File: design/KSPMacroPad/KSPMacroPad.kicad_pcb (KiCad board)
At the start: 2 copper layers, 95.2 x 112.5 mm, 72 parts, among them SW1 SW_Push, SW10 SW_Push, SW11 SW_Push, SW12 SW_Push, SW13 SW_Push, SW14 SW_Push, SW15 SW_Push, SW16 SW_Push, SW17 RotaryEncoder_Switch, SW18 RotaryEncoder_Switch, SW2 SW_Push, SW3 SW_Push, SW4 SW_Push, SW5 SW_Push, SW6 SW_Push, SW7 SW_Push, SW8 SW_Push, SW9 SW_Push, U1 MOUDLE-SEEEDUINO-XIAO

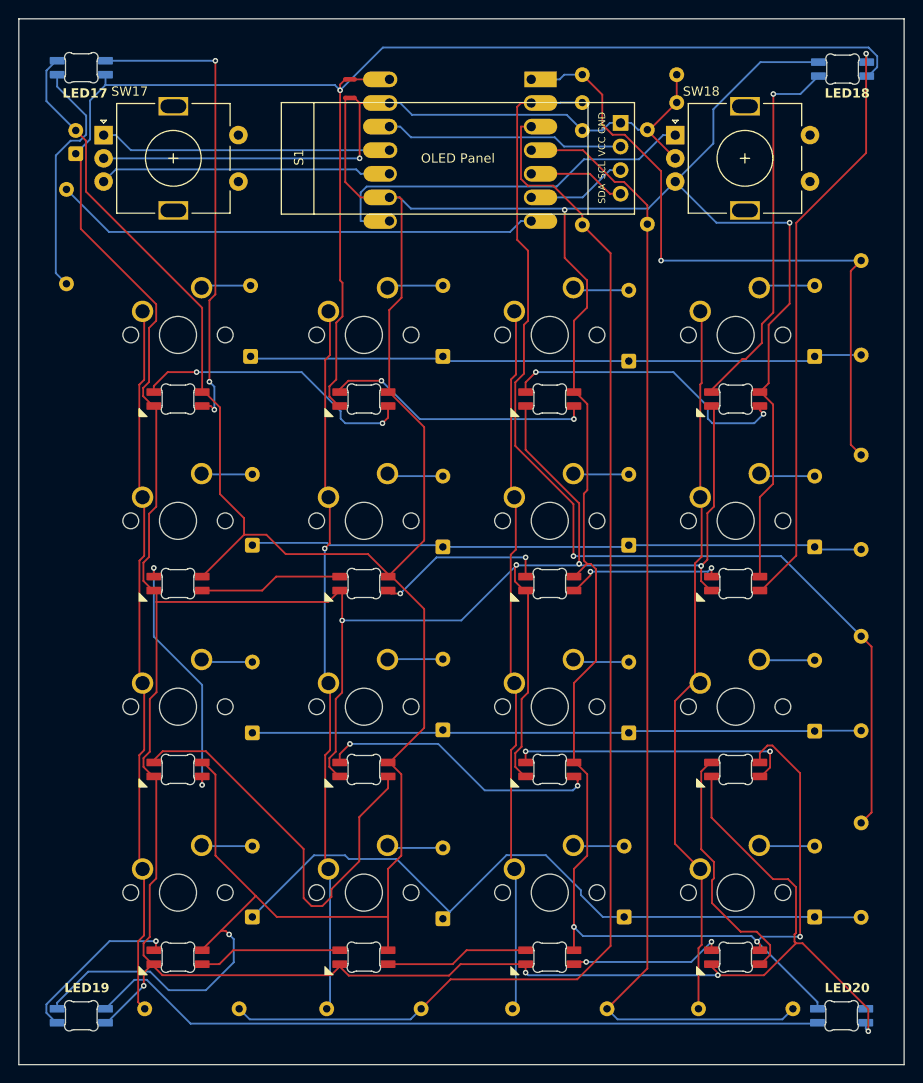
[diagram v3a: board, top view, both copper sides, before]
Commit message: silkscreen and sizine
fixed the sizing of the PCB and added some silkscreen text so the PCB is easier to configure once I build it irl
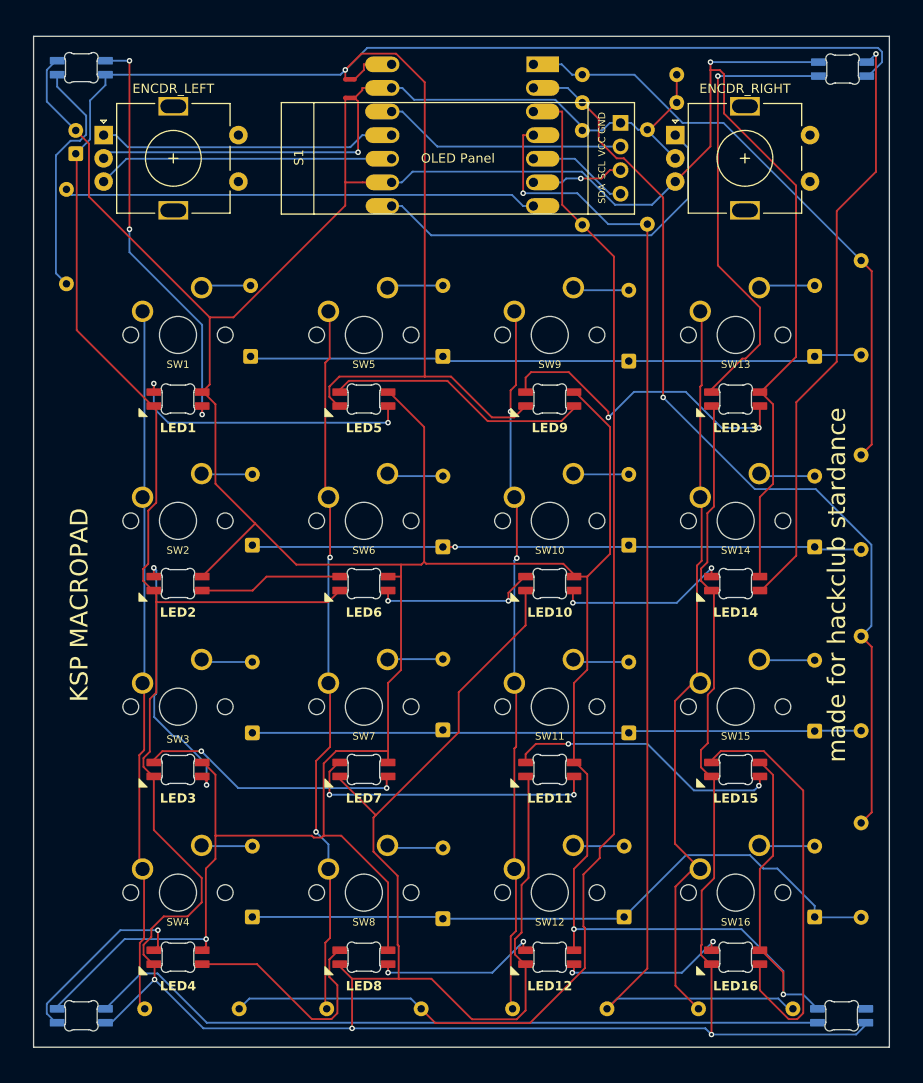
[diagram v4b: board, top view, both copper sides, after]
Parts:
- moved U1 1.63 mm to (115.6, 43.5)
- renumbered SW17 to ENCDR_LEFT, SW18 to ENCDR_RIGHT
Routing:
- net /LED_5V: track 498.6 -> 558.1 mm, vias 9 -> 4
- net Net-(LED15-DOUT): track 27.0 -> 45.3 mm
- net Net-(LED3-DOUT): track 45.7 -> 28.7 mm, vias 0 -> 2
- net /row3_4: track 114.7 -> 102.0 mm
- net Net-(LED4-DIN): track 15.4 -> 24.9 mm
- net Net-(LED13-DOUT): track 40.7 -> 49.1 mm
- net /row1_2: track 73.3 -> 65.9 mm, vias 1 -> 0
- net Net-(LED1-DIN): track 51.3 -> 44.8 mm
- net Net-(D12-K): track 77.4 -> 71.9 mm
- net /col3_4: track 124.1 -> 129.2 mm, vias 0 -> 1
- net Net-(LED13-DIN): track 31.6 -> 34.4 mm
- net Net-(LED12-DOUT): track 15.4 -> 17.9 mm, vias 0 -> 2
- net Net-(R4-Pad1): track 78.7 -> 80.7 mm
- net Net-(LED19-DIN): track 18.2 -> 20.1 mm
- net Net-(LED11-DIN): track 30.4 -> 32.3 mm
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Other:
- board size 95.2 x 112.5 mm -> 92.1 x 108.8 mm
- board text added: "KSP MACROPAD"
- board text added: "a mintythetechman project"
- board text added: "made for hackclub stardance"

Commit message: added M# mounting holes
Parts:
- added SCRW1: MountingHole_3.2mm_M3, MountingHole:MountingHole_3.2mm_M3, F.Cu at (73.5, 68.0)
- added SCRW2: MountingHole_3.2mm_M3, MountingHole:MountingHole_3.2mm_M3, F.Cu at (115.0, 95.5)
- added SCRW3: MountingHole_3.2mm_M3, MountingHole:MountingHole_3.2mm_M3, F.Cu at (158.0, 132.5)
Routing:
- net Net-(LED10-DOUT): track 17.5 -> 19.7 mm

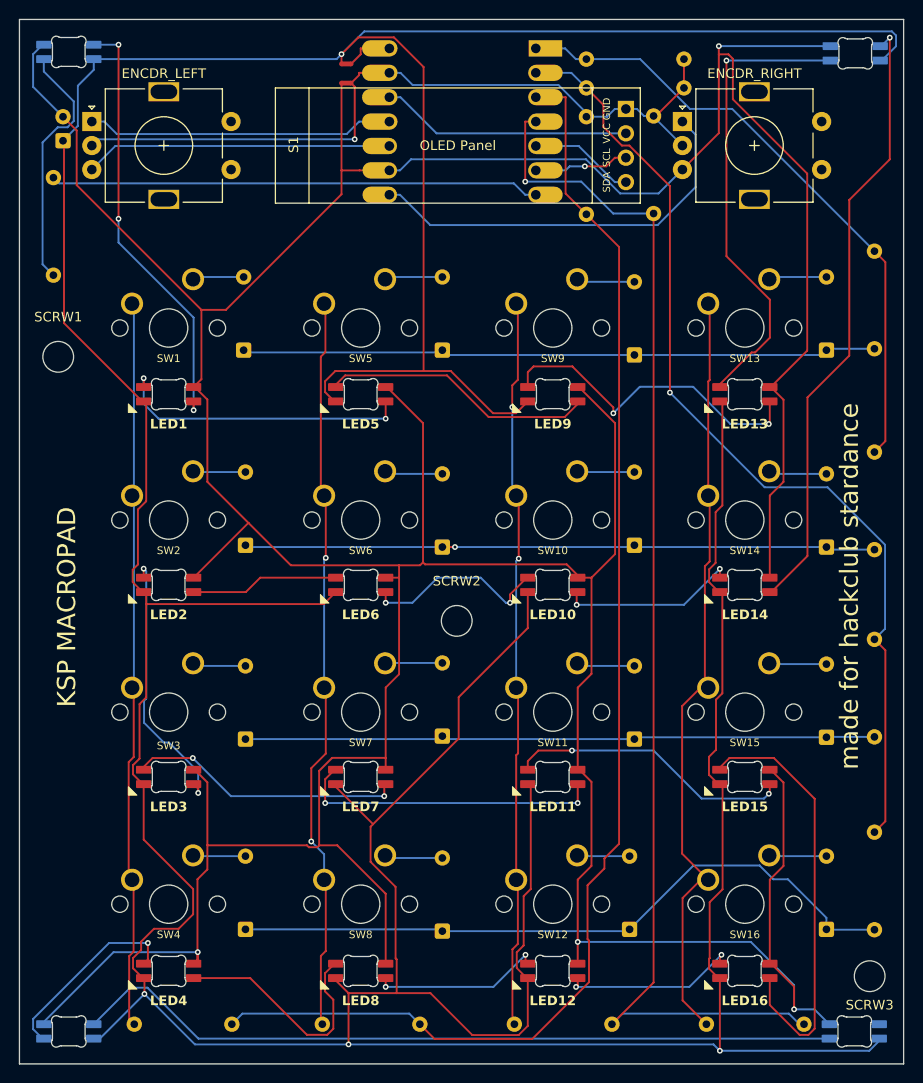
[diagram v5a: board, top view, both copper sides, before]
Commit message: slight sizing change
more rounded numbers for the dimensions of the PCB
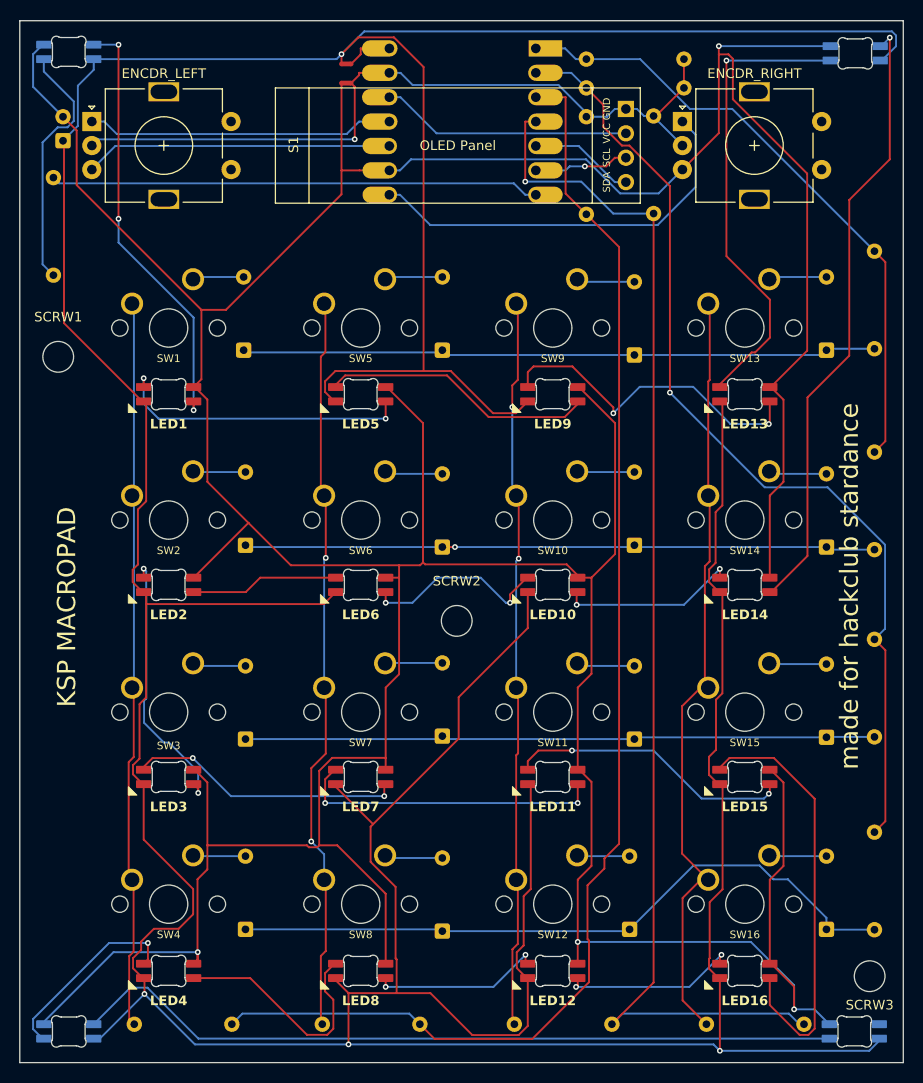
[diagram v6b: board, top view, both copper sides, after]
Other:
- board size 92.1 x 108.8 mm -> 92 x 108.5 mm
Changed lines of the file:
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@@
 	)
 	(gr_rect
-		(start 69.4625 32.8686)
-		(end 161.5375 141.6314)
+		(start 69.5 33)
+		(end 161.5 141.5)
 		(stroke
 			(width 0.05)

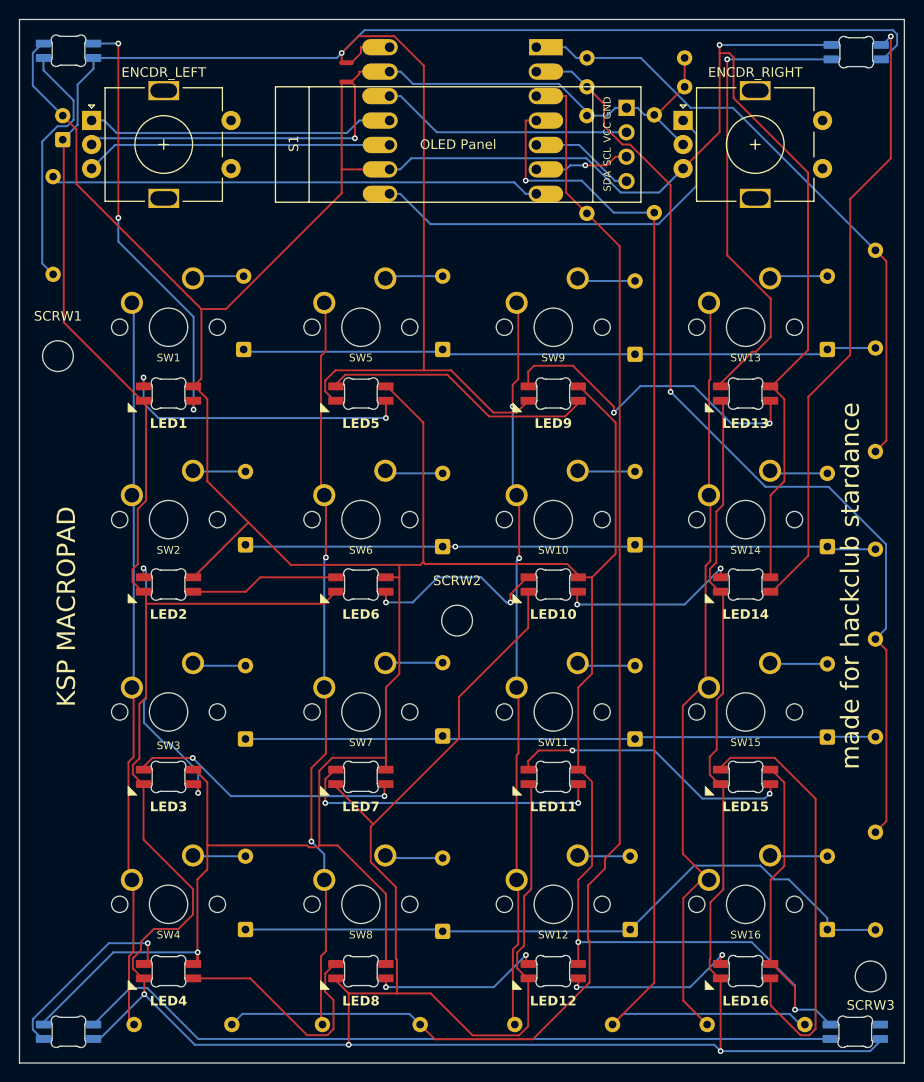
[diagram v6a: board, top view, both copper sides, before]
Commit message: pcb with 3d models
made it so the 3d version of the PCB now has the 3d models
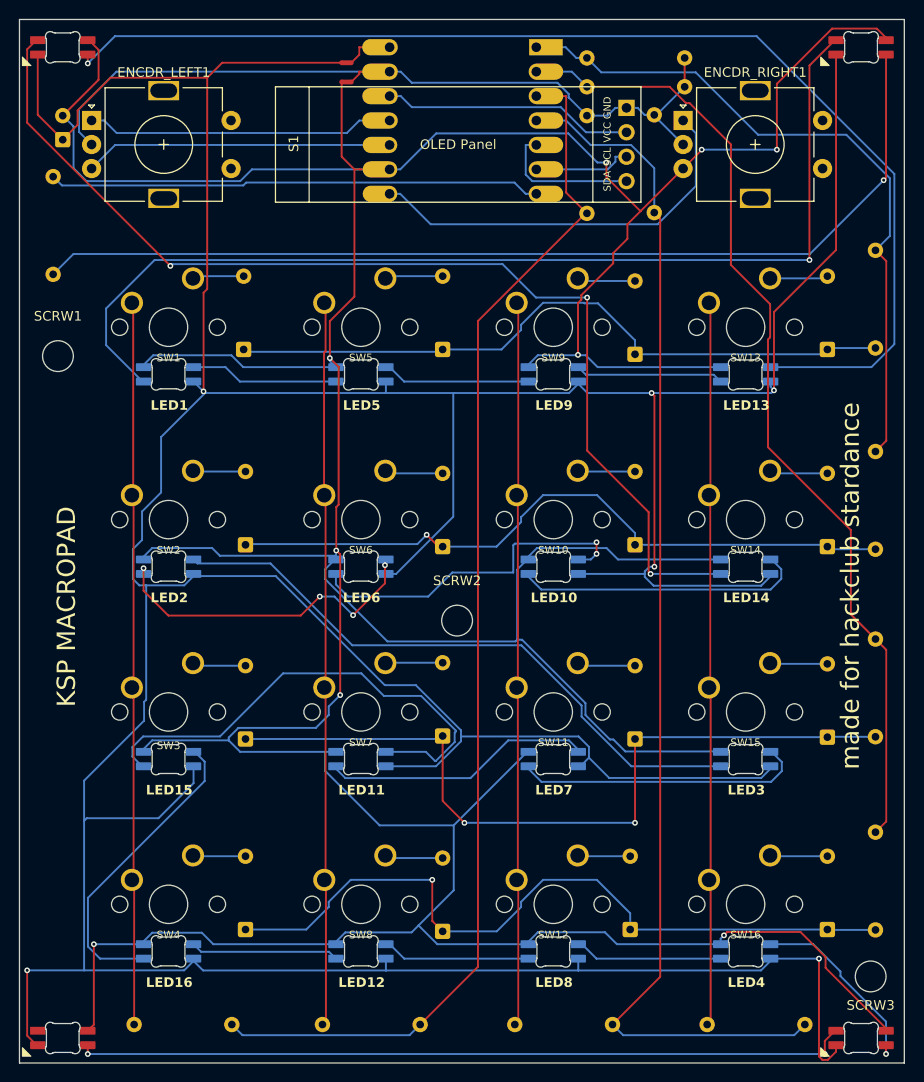
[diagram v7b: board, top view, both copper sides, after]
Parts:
- LED1, LED10, LED11, LED12, LED13, LED14, LED15, LED16, LED2, LED3, LED4, LED5, LED6, LED7, LED8, LED9: footprint footprints:SK6812MINI-E_fixed -> made-for-macro:SK6812MINI-E_fixed; moved to F.Cu
- LED17, LED18, LED19, LED20: footprint footprints:SK6812MINI-E_fixed -> made-for-macro:SK6812MINI-E_fixed; moved to B.Cu
- S1: footprint footprints:SSD1306-0.91-OLED-4pin-128x32 -> made-for-macro:SSD1306-0.91-OLED-4pin-128x32
- U1: footprint footprints:XIAO-Generic-Hybrid-14P-2.54-21X17.8MM -> Seeed-Studio-XIAO-series:XIAO-Generic-Hybrid-14P-2.54-21X17.8MM
- moved LED18 82.5 mm to (74.0, 36.0), turned to 180 degrees
- moved LED19 82.4 mm to (157.0, 139.0), turned to 180 degrees
- moved LED20 82.4 mm to (74.0, 139.0), turned to 180 degrees
- moved LED17 82.4 mm to (157.0, 36.0), turned to 180 degrees
- moved LED16 60.0 mm to (85.0, 130.0), turned to 0 degrees
- moved LED4 60.0 mm to (145.0, 130.0), turned to 0 degrees
- moved LED15 60.0 mm to (85.0, 110.0), turned to 0 degrees
- moved LED3 60.0 mm to (145.0, 110.0), turned to 0 degrees
- moved LED12 20.1 mm to (105.0, 130.0), turned to 0 degrees
- moved LED8 20.1 mm to (125.0, 130.0), turned to 0 degrees
- moved LED11 20.1 mm to (105.0, 110.0), turned to 0 degrees
- moved LED7 20.1 mm to (125.0, 110.0), turned to 0 degrees
- moved LED1 2.00 mm to (85.0, 70.0), turned to 0 degrees
- moved LED13 2.00 mm to (145.0, 70.0), turned to 0 degrees
- moved LED5 2.00 mm to (105.0, 70.0), turned to 0 degrees
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- renumbered ENCDR_LEFT to ENCDR_LEFT1, ENCDR_RIGHT to ENCDR_RIGHT1
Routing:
- net Net-(LED17-DIN): track 26.2 -> 103.6 mm, vias 0 -> 1
- net Net-(LED13-DOUT): track 49.1 -> 123.4 mm
- net Net-(LED1-DIN): track 44.8 -> 108.6 mm, vias 3 -> 1
- net Net-(LED14-DIN): track 64.4 -> 113.8 mm, vias 1 -> 3
- net /LED_5V: track 558.1 -> 517.3 mm, vias 4 -> 6
- net Net-(LED2-DOUT): track 28.3 -> 64.4 mm, vias 2 -> 0
- net Net-(LED11-DOUT): track 29.8 -> 51.4 mm, vias 2 -> 0
- net Net-(LED2-DIN): track 15.4 -> 34.6 mm, vias 0 -> 4
- net Net-(LED13-DIN): track 34.4 -> 15.4 mm, vias 2 -> 0
- net Net-(LED10-DOUT): track 19.7 -> 36.1 mm
- net Net-(D11-K): track 65.9 -> 82.1 mm, vias 0 -> 2
- net /LED_GND: track 516.1 -> 532.1 mm, vias 4 -> 9
- net Net-(LED1-DOUT): track 31.2 -> 15.4 mm, vias 2 -> 0
- net Net-(LED15-DOUT): track 45.3 -> 32.1 mm
- net Net-(LED5-DOUT): track 28.5 -> 15.4 mm
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
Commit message: routing fix
lowk didnt think the routing looked cool enough so I redid it
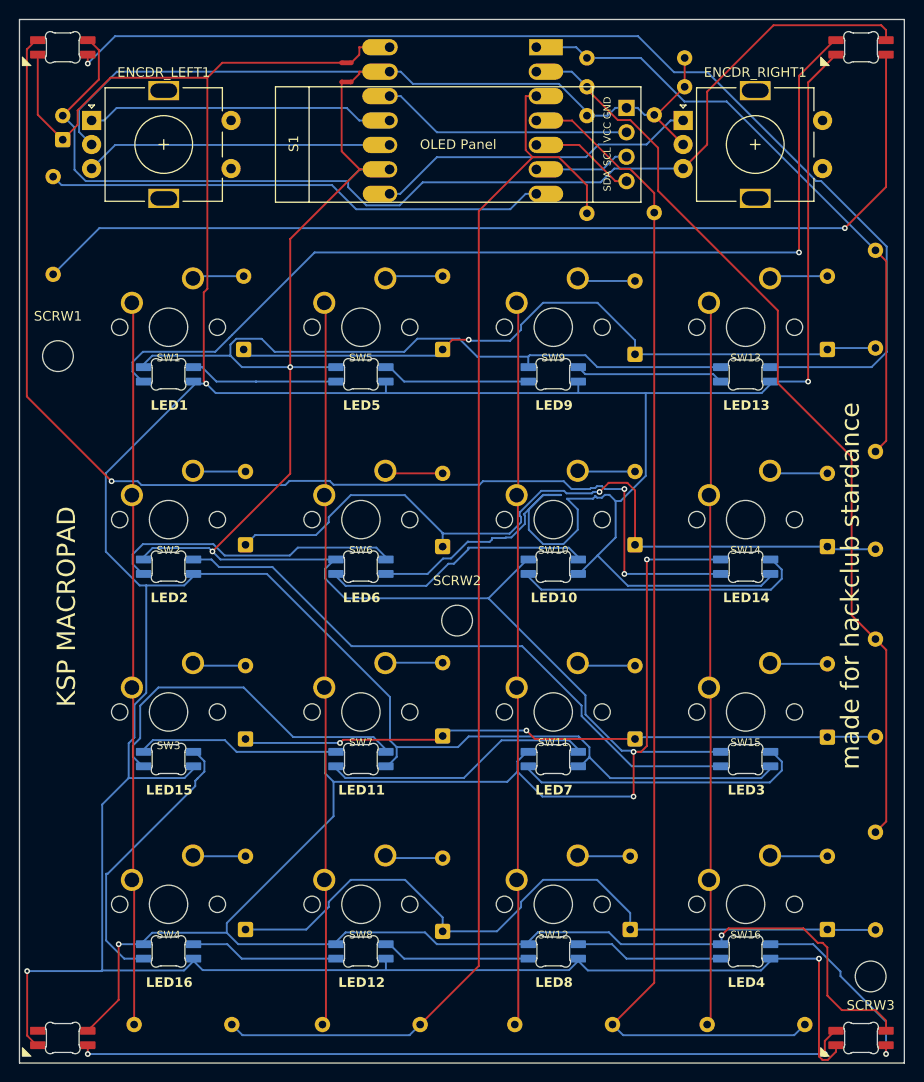
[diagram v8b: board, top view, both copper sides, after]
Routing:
- net /LED_GND: track 532.1 -> 551.1 mm, vias 9 -> 7
- net Net-(D11-K): track 82.1 -> 66.7 mm
- net Net-(LED11-DOUT): track 51.4 -> 36.4 mm
- net /LED_5V: track 517.3 -> 531.3 mm, vias 6 -> 4
- net Net-(LED14-DIN): track 113.8 -> 123.5 mm
- net Net-(U1-PB09_A7_D7_RX): track 42.2 -> 33.7 mm
- net Net-(D10-K): track 72.0 -> 80.4 mm
- net Net-(LED1-DIN): track 108.6 -> 100.3 mm
- net Net-(LED10-DOUT): track 36.1 -> 28.3 mm, vias 2 -> 0
- net /row1_2: track 72.4 -> 65.9 mm
- net Net-(LED13-DOUT): track 123.4 -> 117.9 mm
- net /col1_2: track 128.3 -> 133.1 mm
- net /row3_4: track 102.2 -> 97.5 mm
- net Net-(S1-SDA): track 14.9 -> 10.9 mm
- net Net-(LED2-DIN): track 34.6 -> 30.8 mm, vias 4 -> 0
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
